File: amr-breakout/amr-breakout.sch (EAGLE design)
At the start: 15 parts, among them U1 ZLDO1117G33TC

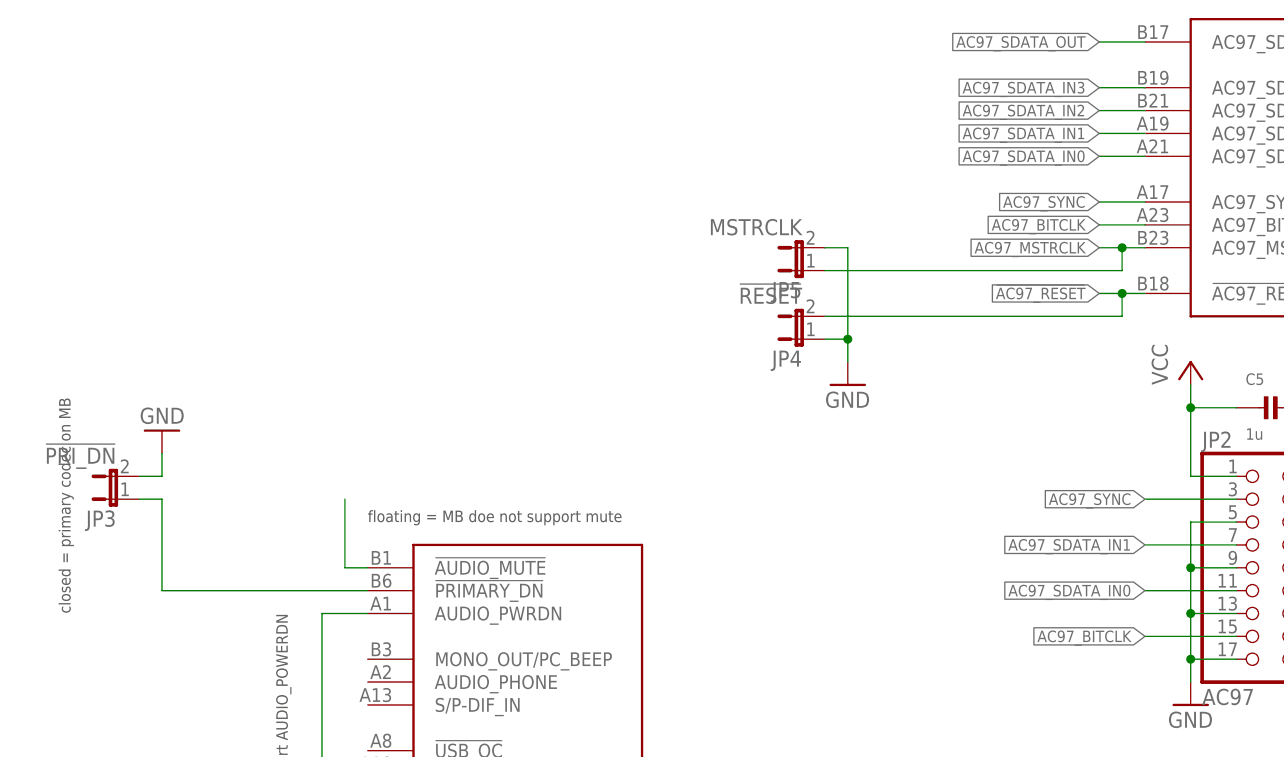
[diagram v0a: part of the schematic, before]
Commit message: amr-breakout: Add pull-ups for !AC97_RESET and !PRIMARY_DN
Closes: OS#5369
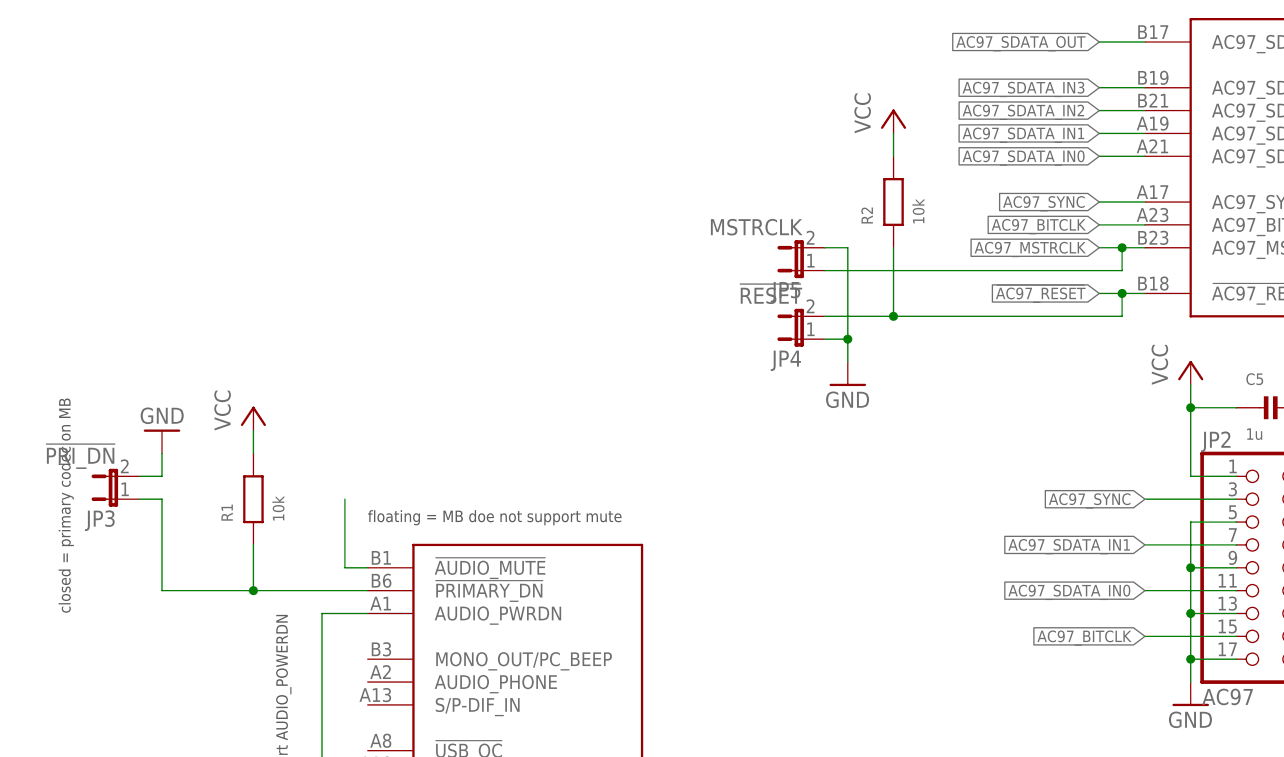
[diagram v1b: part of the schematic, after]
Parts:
- added R1, R2: 10k, rc-sysmocom:RESISTOR_0603
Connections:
- net !AC97_RESET: now also R2.1
- net !PRIMARY_DN: now also R1.1
- net VCC: now also R1.2, R2.2
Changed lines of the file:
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@@
 <part name="JP7" library="pinhead" deviceset="PINHD-1X3" device="" value="12V"/>
 <part name="GND16" library="supply1" deviceset="GND" device=""/>
+<part name="R1" library="rc-sysmocom" deviceset="RESISTOR" device="_0603" value="10k"/>
+<part name="P+1" library="supply1" deviceset="VCC" device=""/>
+<part name="R2" library="rc-sysmocom" deviceset="RESISTOR" device="_0603" value="10k"/>
+<part name="P+5" library="supply1" deviceset="VCC" device=""/>
 </parts>
 <sheets>
@@
 <instance part="JP7" gate="A" x="58.42" y="40.64" rot="R180"/>
 <instance part="GND16" gate="1" x="68.58" y="30.48"/>
+<instance part="R1" gate="G$1" x="114.3" y="111.76" rot="R90"/>
+<instance part="P+1" gate="VCC" x="114.3" y="121.92"/>
+<instance part="R2" gate="G$1" x="185.42" y="144.78" rot="R90"/>
+<instance part="P+5" gate="VCC" x="185.42" y="154.94"/>
 </instances>
 <busses>
@@
 <junction x="88.9" y="68.58"/>
 </segment>
+<segment>
+<pinref part="R1" gate="G$1" pin="2"/>
+<pinref part="P+1" gate="VCC" pin="VCC"/>
+<wire x1="114.3" y1="119.38" x2="114.3" y2="116.84" width="0.1524" layer="91"/>
+</segment>
+<segment>
+<pinref part="R2" gate="G$1" pin="2"/>
+<pinref part="P+5" gate="VCC" pin="VCC"/>
+<wire x1="185.42" y1="152.4" x2="185.42" y2="149.86" width="0.1524" layer="91"/>
+</segment>
 </net>
 <net name="-12V" class="0">
@@
 <wire x1="210.82" y1="134.62" x2="210.82" y2="132.08" width="0.1524" layer="91"/>
 <pinref part="JP4" gate="A" pin="2"/>
-<wire x1="210.82" y1="132.08" x2="177.8" y2="132.08" width="0.1524" layer="91"/>
+<wire x1="210.82" y1="132.08" x2="185.42" y2="132.08" width="0.1524" layer="91"/>
 <junction x="210.82" y="134.62"/>
+<pinref part="R2" gate="G$1" pin="1"/>
+<wire x1="185.42" y1="132.08" x2="177.8" y2="132.08" width="0.1524" layer="91"/>
+<wire x1="185.42" y1="132.08" x2="185.42" y2="139.7" width="0.1524" layer="91"/>
+<junction x="185.42" y="132.08"/>
 </segment>
 <segment>
@@
 <segment>
 <pinref part="U$1" gate="G$1" pin="!PRIMARY_DN"/>
-<wire x1="127" y1="101.6" x2="104.14" y2="101.6" width="0.1524" layer="91"/>
+<wire x1="127" y1="101.6" x2="114.3" y2="101.6" width="0.1524" layer="91"/>
+<wire x1="114.3" y1="101.6" x2="104.14" y2="101.6" width="0.1524" layer="91"/>
 <wire x1="104.14" y1="101.6" x2="104.14" y2="111.76" width="0.1524" layer="91"/>
 <pinref part="JP3" gate="A" pin="1"/>
 <wire x1="104.14" y1="111.76" x2="101.6" y2="111.76" width="0.1524" layer="91"/>
-</segment>
-</net>
+<pinref part="R1" gate="G$1" pin="1"/>
+<wire x1="114.3" y1="101.6" x2="114.3" y2="106.68" width="0.1524" layer="91"/>
+<junction x="114.3" y="101.6"/>
+</segment>
+</net>
